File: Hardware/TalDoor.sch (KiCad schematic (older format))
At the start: 58 parts, among them J1 SI-52003-F_RJ45, J2 Screw_Terminal_01x02, J3 Conn_01x06_Male, J4 Conn_01x06_Male, P1 Conn_02x18_Odd_Even, P2 Conn_02x18_Odd_Even, Q1 RK7002BM, Q2 BSS223PWH6327XTSA1, U1 DRV8837, U2 ENC28J60-I/SO, U3 PN532, U4 AG9700, Y1 25MHz

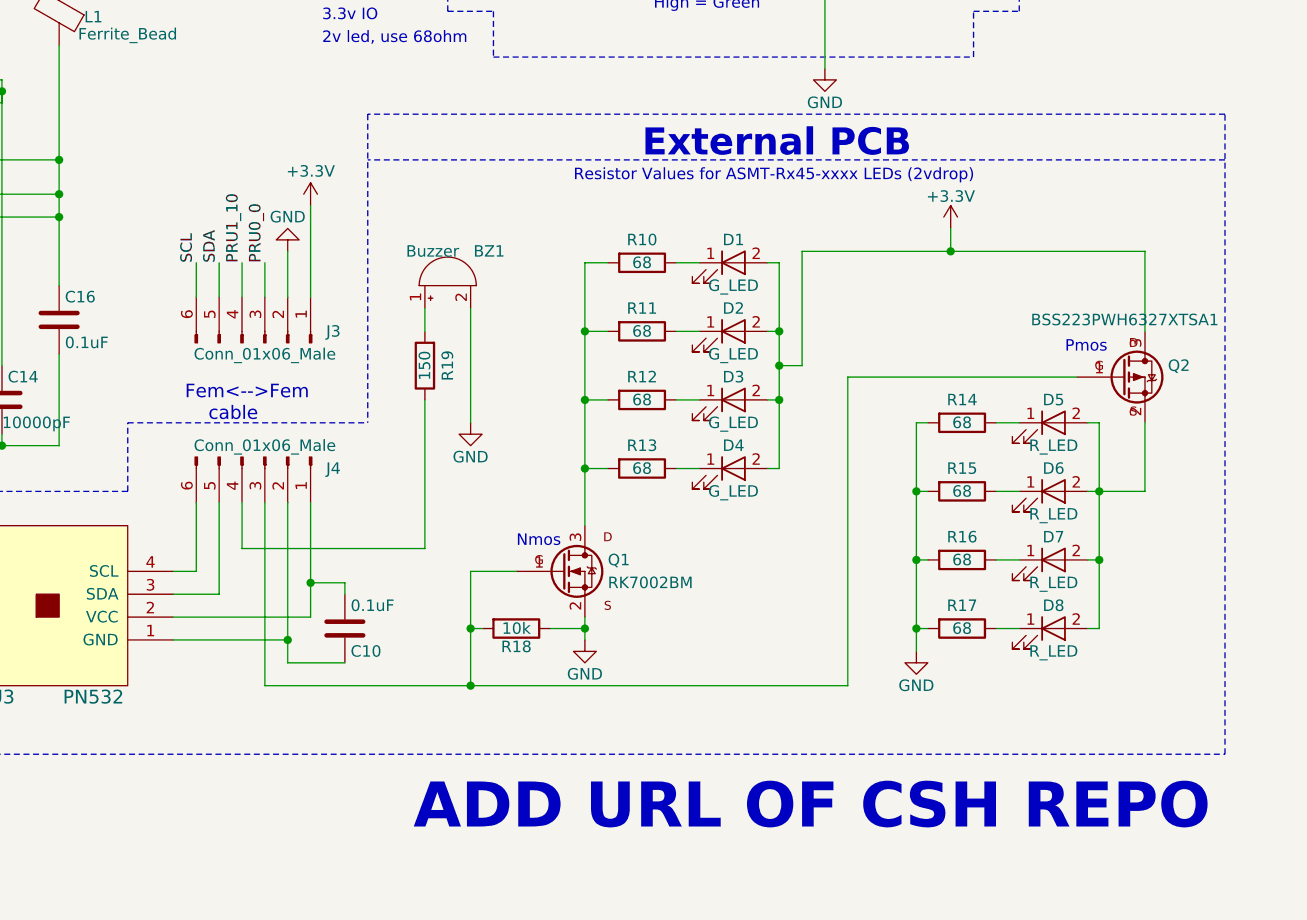
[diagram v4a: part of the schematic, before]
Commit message: Secondary PCB layout complete
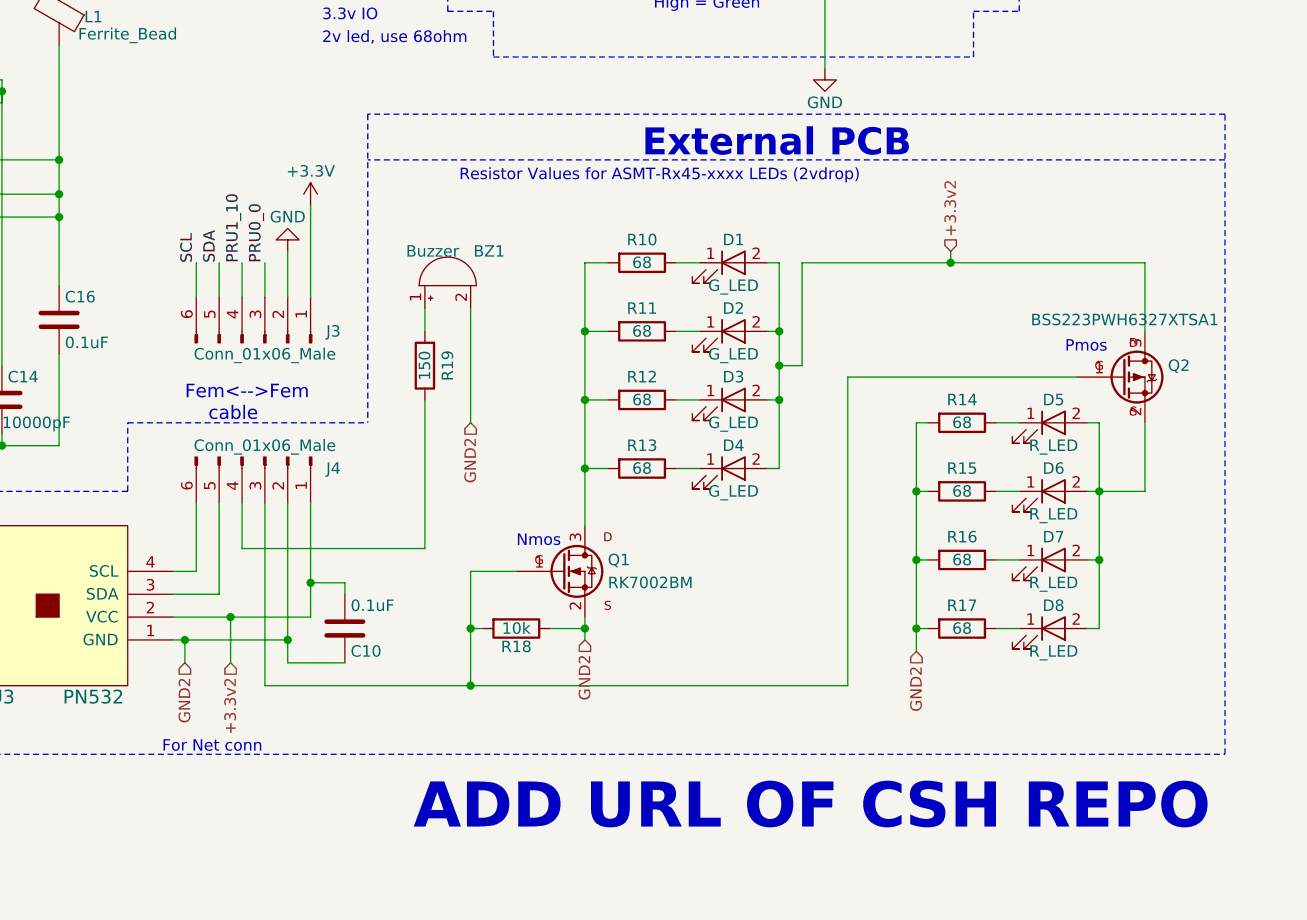
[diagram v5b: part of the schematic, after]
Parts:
- U3: footprint Pin_Headers:Pin_Header_Straight_1x04_Pitch2.54mm -> TalDoor_Footprints:PN532
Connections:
- net +3V3: no longer D1.2 (A), D2.2 (A), D3.2 (A), D4.2 (A), Q2.3 (D)
- net GND: no longer BZ1.2 (+), Q1.2 (S), R14.2, R15.2, R16.2, R17.2, R18.1
- net GND2: now reaches C10.1, J4.2 (Pin_2), U3.1 (GND)
- net GND2: now also BZ1.2 (+), Q1.2 (S), R14.2, R15.2, R16.2, R17.2, R18.1
- net +3.3v2: now reaches C10.2, J4.1 (Pin_1), U3.2 (VCC)
- net +3.3v2: now also D1.2 (A), D2.2 (A), D3.2 (A), D4.2 (A), Q2.3 (D)
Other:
- note added: "For Net conn"
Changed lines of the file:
@@
 F 0 "U3" V 4850 6200 60  0000 C CNN
 F 1 "PN532" V 4850 5800 60  0000 C CNN
-F 2 "Pin_Headers:Pin_Header_Straight_1x04_Pitch2.54mm" H 5250 6050 60  0001 C CNN
+F 2 "TalDoor_Footprints:PN532" H 5250 6050 60  0001 C CNN
 F 3 "" H 5250 6050 60  0001 C CNN
 	1    5250 6050
@@
 	0    1    1    0
 $EndComp
-Text Notes 7600 4200 0    50   ~ 0
+Text Notes 7100 4200 0    50   ~ 0
 Resistor Values for ASMT-Rx45-xxxx LEDs (2vdrop)
 $Comp
@@
 	-1   0    0    1
 $EndComp
-$Comp
-L GND #PWR011
-U 1 1 5A4876A4
-P 7150 5250
-F 0 "#PWR011" H 7150 5000 50  0001 C CNN
-F 1 "GND" H 7150 5100 50  0000 C CNN
-F 2 "" H 7150 5250 50  0001 C CNN
-F 3 "" H 7150 5250 50  0001 C CNN
-	1    7150 5250
-	1    0    0    -1
-$EndComp
 Text Notes 7900 4100 0    118  ~ 24
 External PCB
 $Comp
-L +3.3V #PWR012
+L +3.3V #PWR011
 U 1 1 5A489389
 P 2850 6550
-F 0 "#PWR012" H 2850 6400 50  0001 C CNN
+F 0 "#PWR011" H 2850 6400 50  0001 C CNN
 F 1 "+3.3V" H 2850 6690 50  0000 C CNN
 F 2 "" H 2850 6550 50  0001 C CNN
@@
 $EndComp
 $Comp
-L GND #PWR013
+L GND #PWR012
 U 1 1 5A48981F
 P 1550 7600
-F 0 "#PWR013" H 1550 7350 50  0001 C CNN
+F 0 "#PWR012" H 1550 7350 50  0001 C CNN
 F 1 "GND" H 1550 7450 50  0000 C CNN
 F 2 "" H 1550 7600 50  0001 C CNN
@@
 Door Drive Rev
 $Comp
-L +3.3V #PWR014
+L +3.3V #PWR013
 U 1 1 5A48A4FE
 P 1550 6550
-F 0 "#PWR014" H 1550 6400 50  0001 C CNN
+F 0 "#PWR013" H 1550 6400 50  0001 C CNN
 F 1 "+3.3V" H 1550 6690 50  0000 C CNN
 F 2 "" H 1550 6550 50  0001 C CNN
@@
 $EndComp
 $Comp
-L GND #PWR015
+L GND #PWR014
 U 1 1 5A48CC41
 P 1350 7000
-F 0 "#PWR015" H 1350 6750 50  0001 C CNN
+F 0 "#PWR014" H 1350 6750 50  0001 C CNN
 F 1 "GND" H 1350 6850 50  0000 C CNN
 F 2 "" H 1350 7000 50  0001 C CNN
@@
 $EndComp
 $Comp
-L GND #PWR016
+L GND #PWR015
 U 1 1 5A48CCD9
 P 3100 7000
-F 0 "#PWR016" H 3100 6750 50  0001 C CNN
+F 0 "#PWR015" H 3100 6750 50  0001 C CNN
 F 1 "GND" H 3100 6850 50  0000 C CNN
 F 2 "" H 3100 7000 50  0001 C CNN
@@
 Low = Red\nHigh = Green
 $Comp
-L +3.3V #PWR017
-U 1 1 5A4D8685
-P 9250 4400
-F 0 "#PWR017" H 9250 4250 50  0001 C CNN
-F 1 "+3.3V" H 9250 4540 50  0000 C CNN
-F 2 "" H 9250 4400 50  0001 C CNN
-F 3 "" H 9250 4400 50  0001 C CNN
-	1    9250 4400
-	1    0    0    -1
-$EndComp
-$Comp
 L RK7002BM Q1
 U 1 1 5A4D88E6
@@
 $EndComp
 $Comp
-L GND #PWR018
-U 1 1 5A4D88ED
-P 7650 6200
-F 0 "#PWR018" H 7650 5950 50  0001 C CNN
-F 1 "GND" H 7650 6050 50  0000 C CNN
-F 2 "" H 7650 6200 50  0001 C CNN
-F 3 "" H 7650 6200 50  0001 C CNN
-	1    7650 6200
-	1    0    0    -1
-$EndComp
-$Comp
 L R R18
 U 1 1 5A4D88F3
@@
 $EndComp
 $Comp
-L +3.3V #PWR019
+L +3.3V #PWR016
 U 1 1 5A4E00F4
 P 6450 4300
-F 0 "#PWR019" H 6450 4150 50  0001 C CNN
+F 0 "#PWR016" H 6450 4150 50  0001 C CNN
 F 1 "+3.3V" H 6450 4450 50  0000 C CNN
 F 2 "" H 6450 4300 50  0001 C CNN
@@
 $EndComp
 $Comp
-L GND #PWR020
+L GND #PWR017
 U 1 1 5A4E04EF
 P 6350 4500
-F 0 "#PWR020" H 6350 4250 50  0001 C CNN
+F 0 "#PWR017" H 6350 4250 50  0001 C CNN
 F 1 "GND" H 6350 4350 50  0000 C CNN
 F 2 "" H 6350 4500 50  0001 C CNN
@@
 	1    0    0    -1
 $EndComp
+Text Notes 9750 4950 0    50   ~ 0
+Pmos
+Text Notes 7350 5800 0    50   ~ 0
+Nmos
 Wire Notes Line
 	7050 1450 7050 3450
@@
 Connection ~ 9900 5850
 Wire Wire Line
-	10100 4500 10100 4850
+	10100 4550 10100 4850
 Wire Wire Line
 	10100 5550 10100 5250
 Wire Wire Line
-	8600 4500 10100 4500
-Wire Wire Line
-	9250 4500 9250 4400
-Wire Wire Line
-	8600 5000 8600 4500
-Connection ~ 9250 4500
+	8600 4550 10100 4550
+Wire Wire Line
+	9250 4550 9250 4500
+Wire Wire Line
+	8600 5000 8600 4550
+Connection ~ 9250 4550
 Wire Wire Line
 	9800 5050 8800 5050
@@
 	7650 6100 7650 6200
 Connection ~ 9100 6150
-$Comp
-L GND #PWR021
-U 1 1 5A504C42
-P 9100 6250
-F 0 "#PWR021" H 9100 6000 50  0001 C CNN
-F 1 "GND" H 9100 6100 50  0000 C CNN
-F 2 "" H 9100 6250 50  0001 C CNN
-F 3 "" H 9100 6250 50  0001 C CNN
-	1    9100 6250
-	1    0    0    -1
-$EndComp
 Wire Wire Line
 	9150 6150 9100 6150
@@
 	7200 6150 7150 6150
 Connection ~ 7150 6150
-Text Notes 9750 4950 0    50   ~ 0
-Pmos
-Text Notes 7350 5800 0    50   ~ 0
-Nmos
+Wire Wire Line
+	5900 6300 5900 6200
+Connection ~ 5900 6200
+Wire Wire Line
+	6100 6300 6100 6100
+Connection ~ 6100 6100
+Text Notes 5800 6700 0    50   ~ 0
+For Net conn
+Text HLabel 6100 6300 3    50   Input ~ 0
++3.3v2
+Text HLabel 9250 4500 1    50   Input ~ 0
++3.3v2
+Text HLabel 5900 6300 3    50   Input ~ 0
+GND2
+Text HLabel 7150 5250 3    50   Input ~ 0
+GND2
+Text HLabel 9100 6250 3    50   Input ~ 0
+GND2
+Text HLabel 7650 6200 3    50   Input ~ 0
+GND2
 $EndSCHEMATC

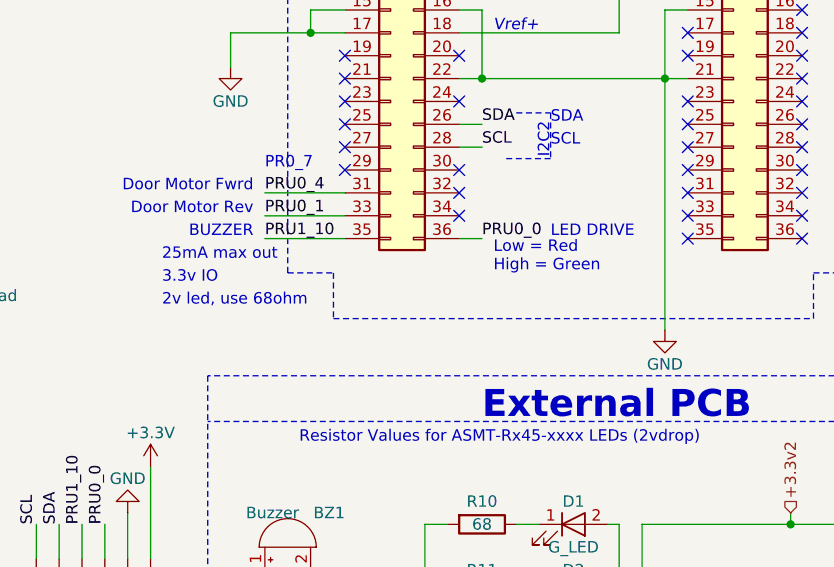
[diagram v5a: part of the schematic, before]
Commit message: adding measurements for main PCB
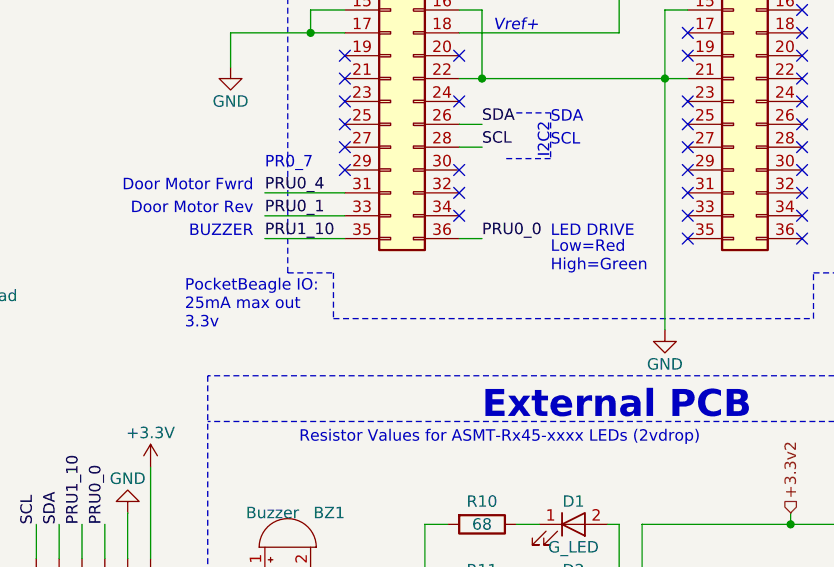
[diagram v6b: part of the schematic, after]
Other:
- note added: "Low=Red\nHigh=Green"
- note added: "PocketBeagle IO:\n25mA max out\n3.3v"
- note removed: "25mA max out"
- note removed: "2v led, use 68ohm\n"
- note removed: "3.3v IO"
- note removed: "Low = Red\nHigh = Green"
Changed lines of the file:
@@
 Text Label 6950 3100 0    50   ~ 0
 PRU0_4
-Text Notes 6500 3400 0    50   ~ 0
-25mA max out
-Text Notes 6500 3500 0    50   ~ 0
-3.3v IO
-Text Notes 6500 3600 0    50   ~ 0
-2v led, use 68ohm\n
+Text Notes 6600 3700 0    50   ~ 0
+PocketBeagle IO:\n25mA max out\n3.3v
 Text Notes 6900 3300 2    50   ~ 0
 BUZZER
@@
 Text Label 2750 7350 0    50   ~ 0
 PRU0_4
-Text Notes 7950 3450 0    50   ~ 0
-Low = Red\nHigh = Green
+Text Notes 8200 3450 0    50   ~ 0
+Low=Red\nHigh=Green
 $Comp
 L RK7002BM Q1

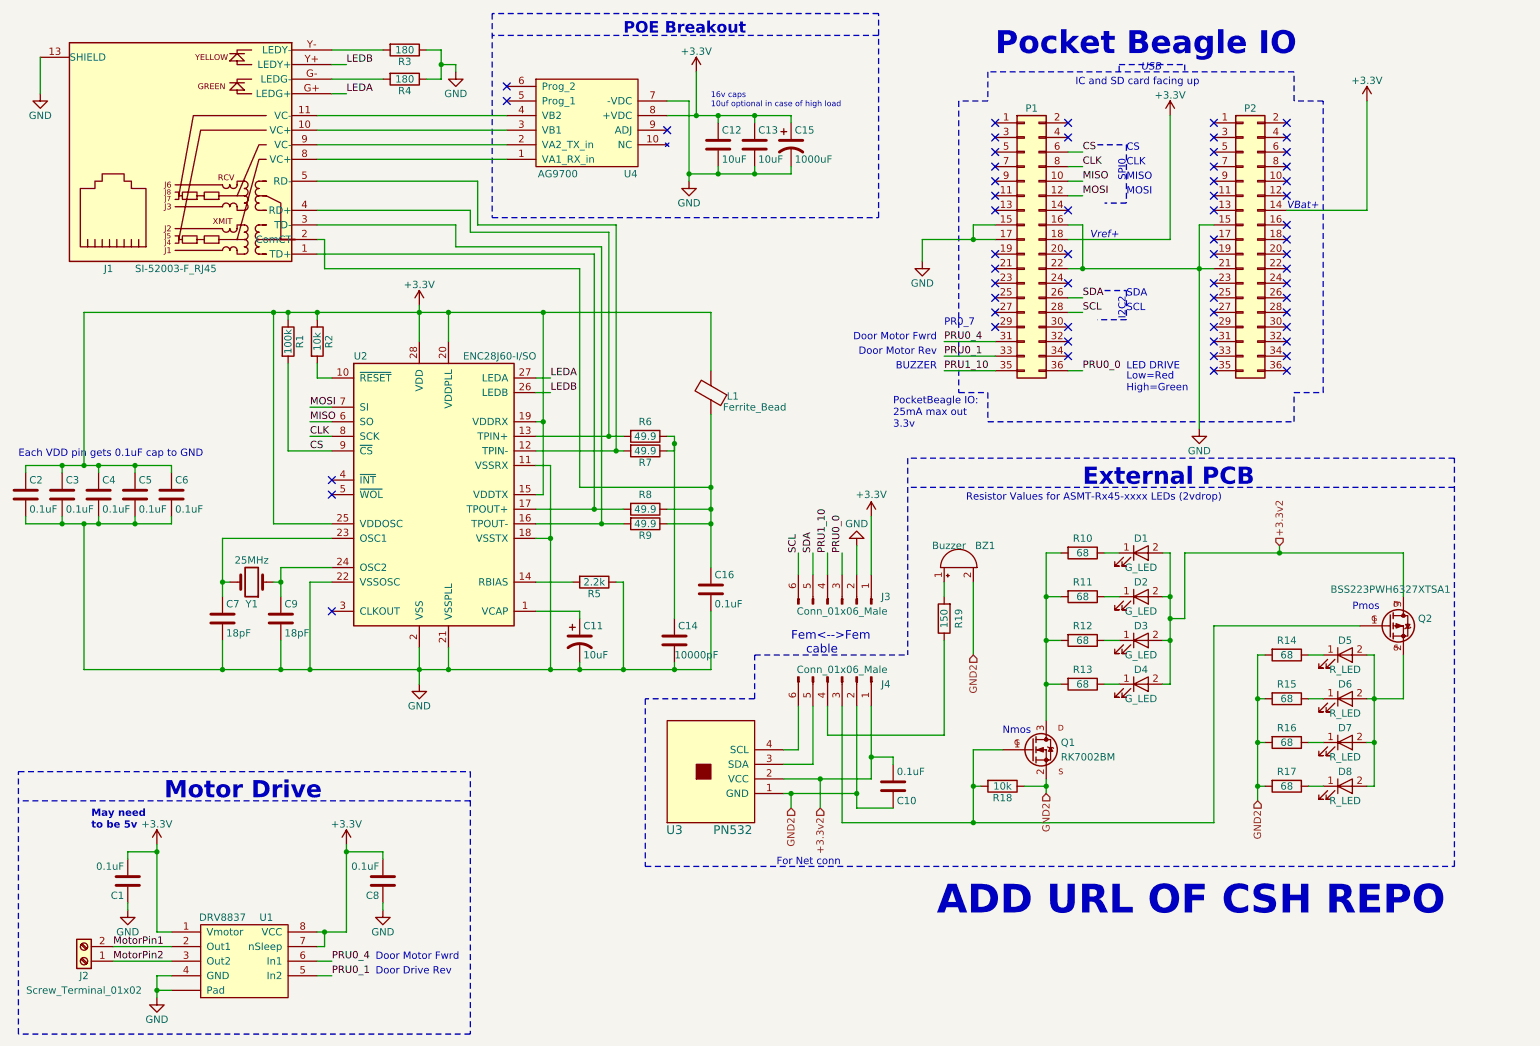
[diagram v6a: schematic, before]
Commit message: Completed Mainboard PCB, needs Vgroove/Mousebite connection between two. Also check motor driver
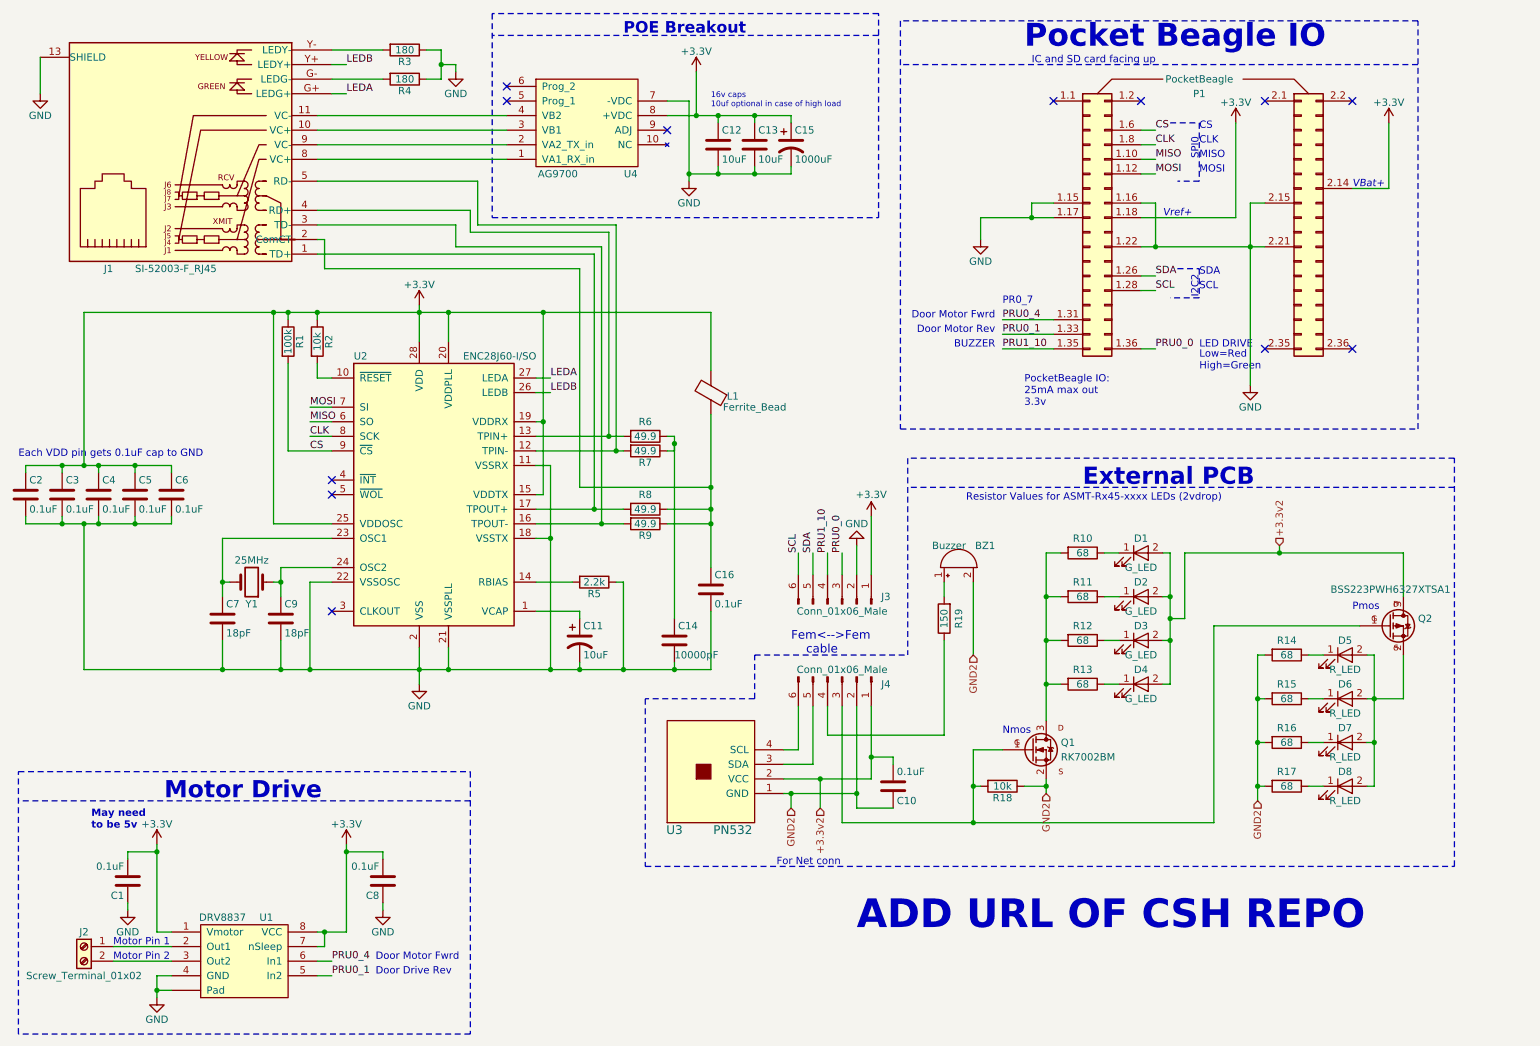
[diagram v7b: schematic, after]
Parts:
- removed P1, P2: Conn_02x18_Odd_Even, Pin_Headers:Pin_Header_Straight_2x18_Pitch2.54mm, symbol Conn_02x18_Odd_Even
- added P1: PocketBeagle, TalDoor_Footprints:PocketBeagle_TalDoor, symbol PocketBeagle
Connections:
- net +3V3: now also P1.1.18 (Pin_18), P1.2.14 (Pin_14)
- net CLK: now also P1.1.8 (Pin_8)
- net CS: now also P1.1.6 (Pin_6)
- net GND: now also P1.1.15 (Pin_15), P1.1.16 (Pin_16), P1.1.17 (Pin_17), P1.1.22 (Pin_25), P1.2.15 (Pin_15), P1.2.21 (Pin_21)
- net MISO: now also P1.1.10 (Pin_10)
- net MOSI: now also P1.1.12 (Pin_12)
- net PRU0_0: now also P1.1.36 (Pin_36)
- net PRU0_1: now also P1.1.33 (Pin_33)
- net PRU0_4: now also P1.1.31 (Pin_31)
- net PRU1_10: now also P1.1.35 (Pin_35)
- net SCL: now also P1.1.28 (Pin_28)
- net SDA: now also P1.1.26 (Pin_26)
- net MotorPin1: no longer names the net of U1.2 (Out1)
- net MotorPin1: now also J2.1 (Pin_1); no longer J2.2 (Pin_2)
- net MotorPin2: no longer names the net of U1.3 (Out2)
- net MotorPin2: now also J2.2 (Pin_2); no longer J2.1 (Pin_1)
- no-connect marks 60 -> 12
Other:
- note added: "Motor Pin 1\n"
- note added: "Motor Pin 2\n"
- note removed: "USB\n"
